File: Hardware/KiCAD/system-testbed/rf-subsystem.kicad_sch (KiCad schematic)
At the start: 42 parts, among them P3 Conn_Coaxial_UHF, U3 CC1200RHBR, U4 SKY13380-350LF, X1 40 MHz

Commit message: feat: begin dedicated sheets for RF switch throws, refine PA RFIC symbol #34
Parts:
- removed U4: SKY13380-350LF, Package_DFN_QFN:QFN-16-1EP_3x3mm_P0.5mm_EP1.7x1.7mm, symbol RF_Switch:SKY13380-350LF
- added FL1: LFCN-490, Filter:Filter_Mini-Circuits_FV1206, symbol RF_Filter:LFCN-490
- added FL2: LFCN-160, Filter:Filter_Mini-Circuits_FV1206, symbol RF_Filter:LFCN-160
- P3: value Conn_Coaxial_UHF -> SMA
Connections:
- net RF_{TRX} is gone; now on an unnamed net: C177.2, L174.2
- net VDD is gone; now on net +3.3V: C171.1, C172.1, C173.1, R171.1
- net GND: now also FL1.2 (GND), FL1.4 (GND), FL2.2 (GND), FL2.4 (GND)
- net UHF 6W PA/RF_{OUT}: now also FL1.1 (IN)
- net RF Switch/RFSW_{POLE}: now reaches P3.1 (In)
- net RF Switch/RFSW_{POLE}: no longer R181.1
- net RF_Signal: no longer names the net of R181.2
- new net TRX_{RF}: R181.1
- new net TX_{UHF}: FL1.3 (OUT)
- new net TX_{VHF}: FL2.3 (OUT)
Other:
- sheet RF Power Amplifier renamed UHF 6W PA
- added sheet RF Switch (rf-switch.kicad_sch)
- added sheet VHF 6W PA (rf-power-amplifier-vhf.kicad_sch)
- sheet UHF 6W PA: file rf-power-amplifier.kicad_sch -> rf-power-amplifier-uhf.kicad_sch
- note added: "RF Frontend for UHF Reference 420-470 MHz Tune"
- note added: "TRX_GPIO3 can be used to control an external LNA, PA, or RX/TX switch. HIGH in Sleep, Active LOW"
- note removed: "Antenna"
- note removed: "RF Frontend"
- note removed: "TRX_GPIO3 can be used to control an external LNA, PA, or RX/TX switch."
- moved on the sheet: P3, R181

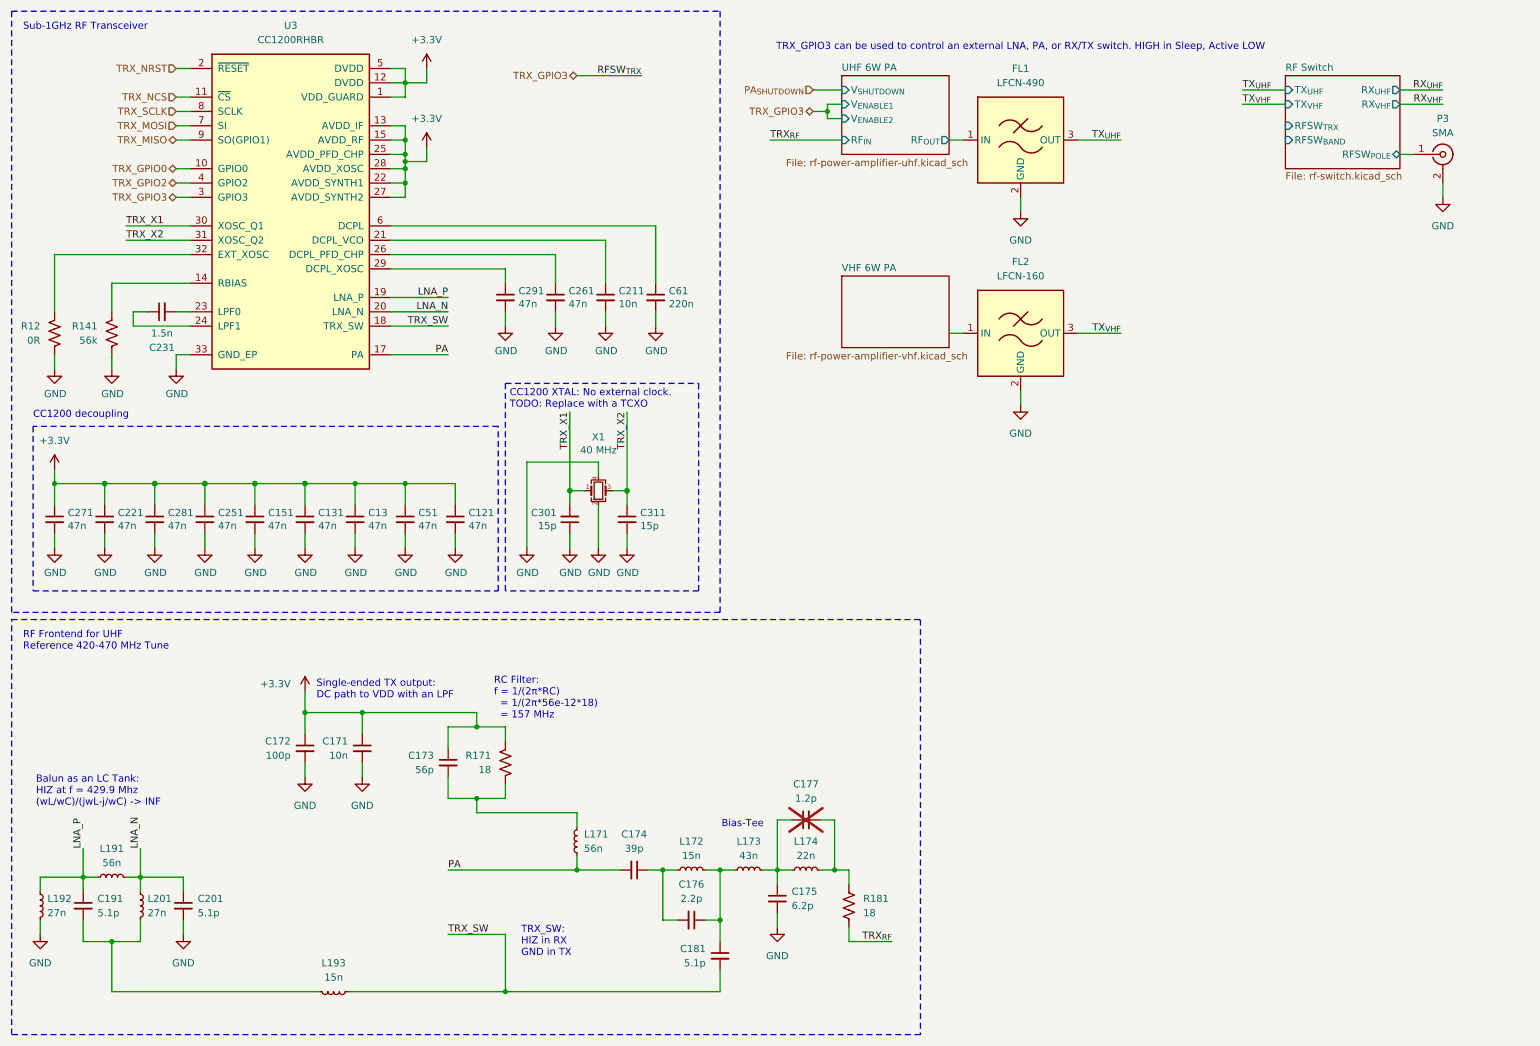
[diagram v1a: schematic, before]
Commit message: feat: refine rf subsystem sheet, specify band selection from two tuned PAs #34
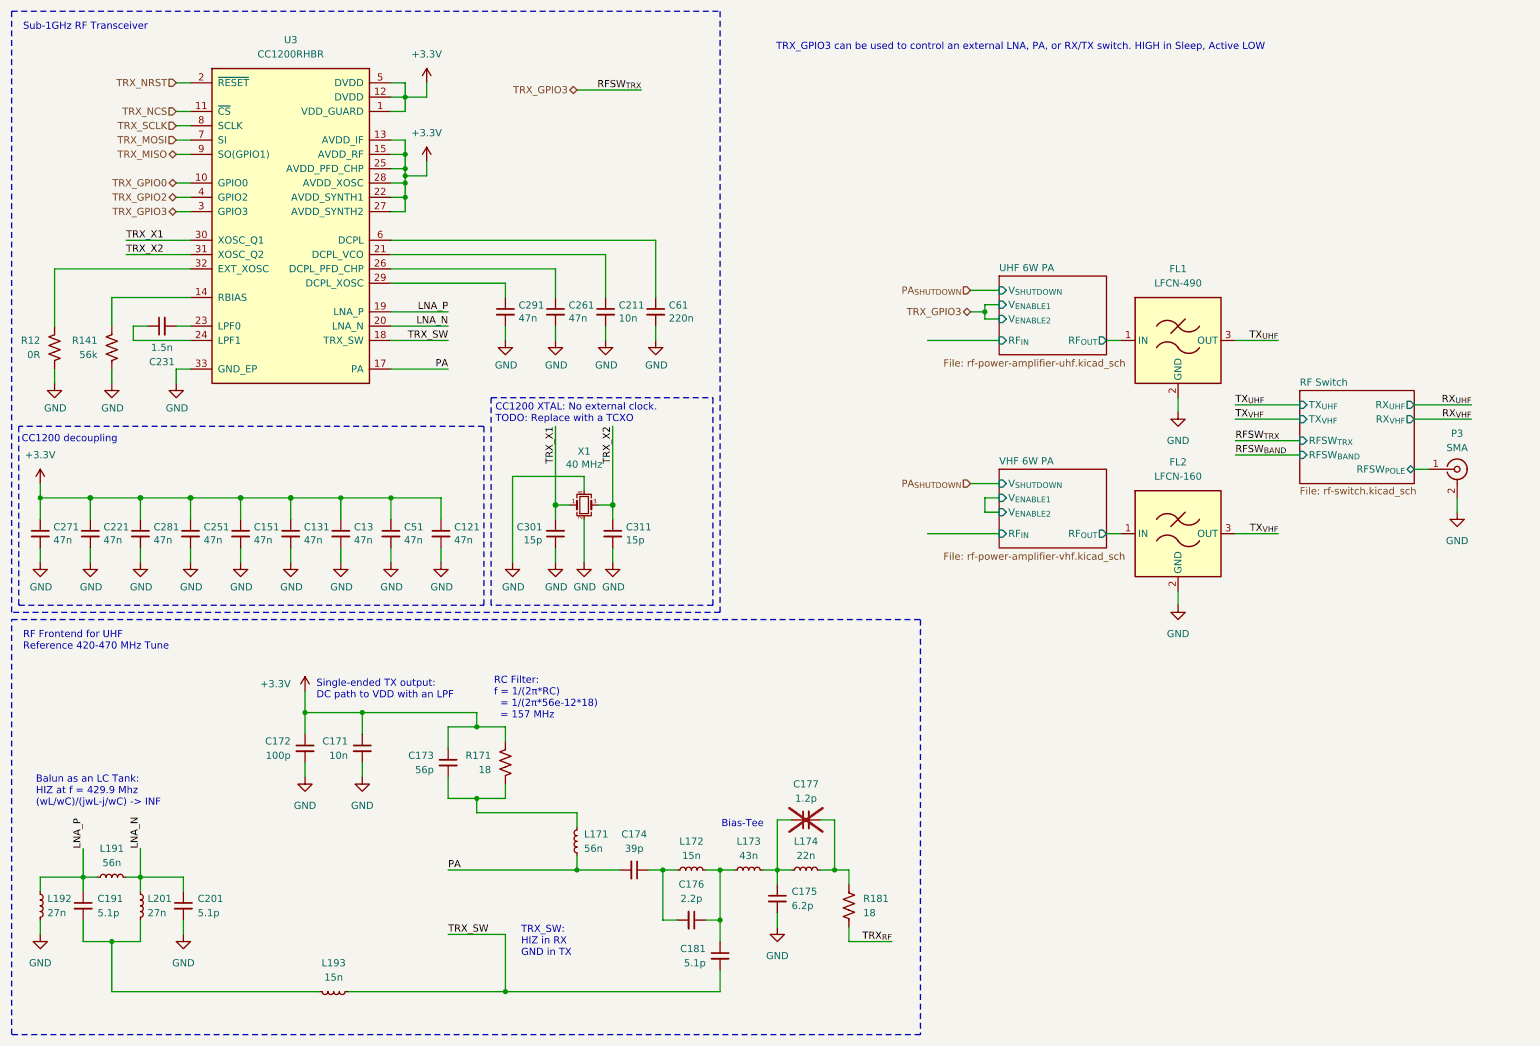
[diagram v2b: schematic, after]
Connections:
- net VHF 6W PA/RF_{OUT}: now reaches FL2.1 (IN)
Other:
- sheet VHF 6W PA ports: added RF_{IN}, RF_{OUT}, V_{ENABLE1}, V_{ENABLE2}, V_{SHUTDOWN}; removed none
- moved on the sheet: C121, C13, C131, C151, C211, C221, C231, C251, C261, C271, C281, C291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

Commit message: feat: complete RF switches, revise RF sheet structure #34
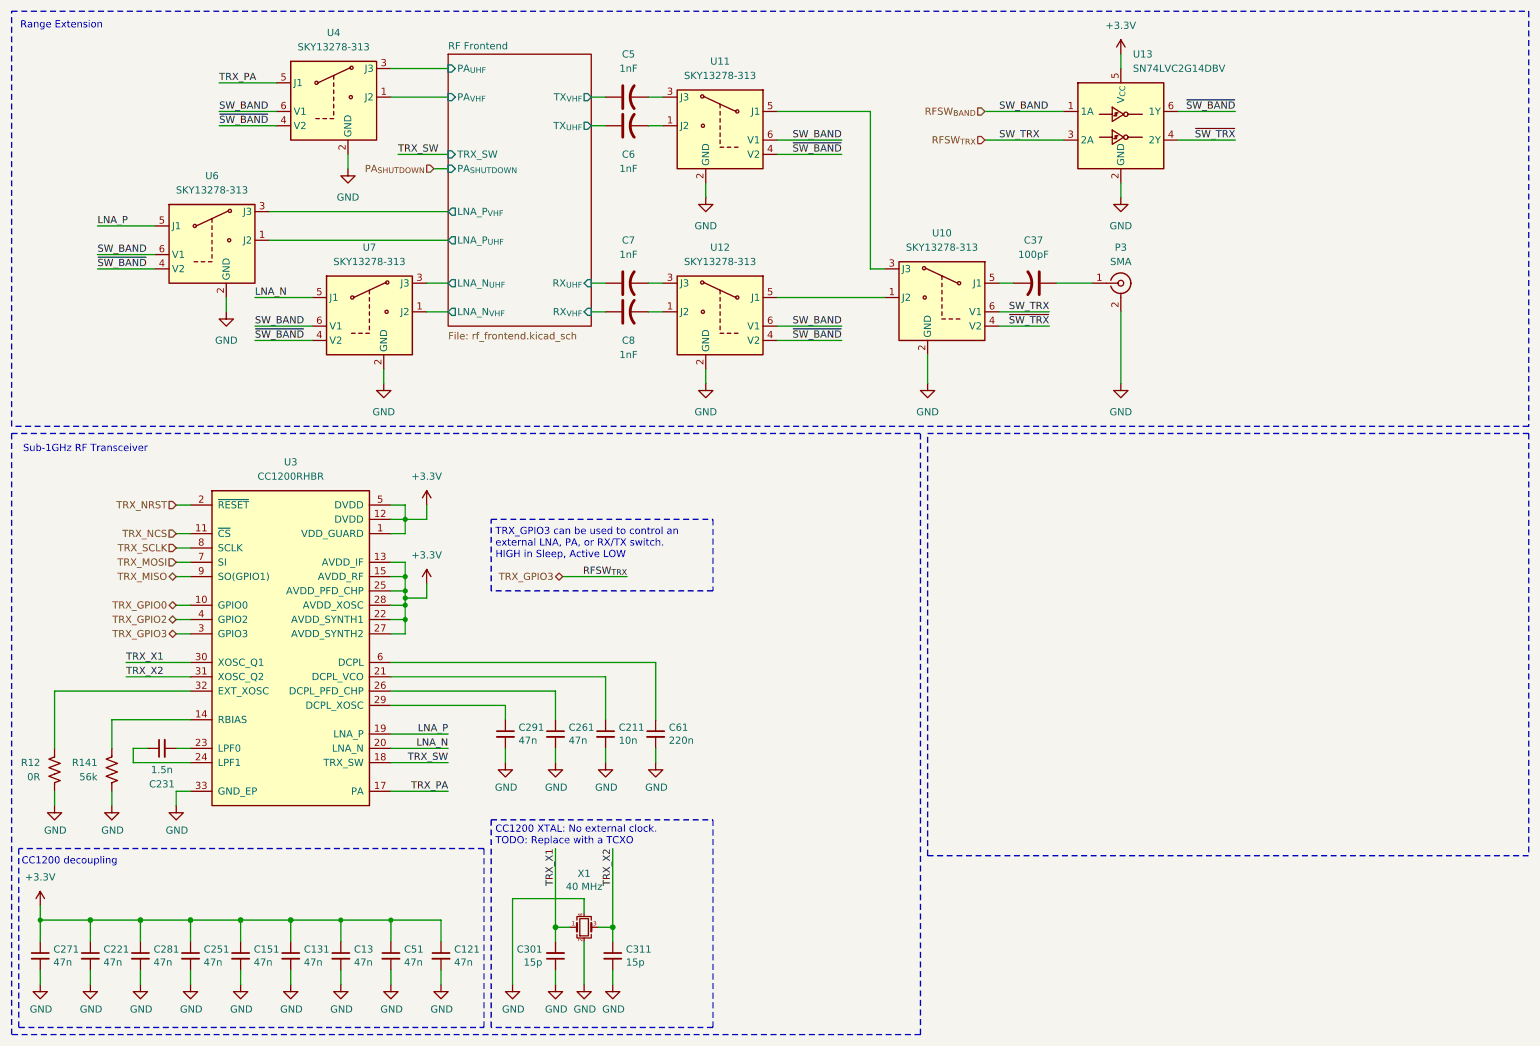
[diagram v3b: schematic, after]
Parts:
- removed C171: 10n, Capacitor_SMD:C_0402_1005Metric, symbol Device:C_Small
- removed C172: 100p, Capacitor_SMD:C_0402_1005Metric, symbol Device:C_Small
- removed C173: 56p, Capacitor_SMD:C_0402_1005Metric, symbol Device:C_Small
- removed C174: 39p, Capacitor_SMD:C_0402_1005Metric, symbol Device:C_Small
- removed C175: 6.2p, Capacitor_SMD:C_0402_1005Metric, symbol Device:C_Small
- removed C176: 2.2p, Capacitor_SMD:C_0402_1005Metric, symbol Device:C_Small
- removed C177: 1.2p, Capacitor_SMD:C_0402_1005Metric, symbol Device:C_Small
- removed C181, C191, C201: 5.1p, Capacitor_SMD:C_0402_1005Metric, symbol Device:C_Small
- removed FL1: LFCN-490, Filter:Filter_Mini-Circuits_FV1206, symbol RF_Filter:LFCN-490
- removed FL2: LFCN-160, Filter:Filter_Mini-Circuits_FV1206, symbol RF_Filter:LFCN-160
- removed L171, L191: 56n, Inductor_SMD:L_0402_1005Metric, symbol Device:L_Small
- removed L172, L193: 15n, Inductor_SMD:L_0402_1005Metric, symbol Device:L_Small
- removed L173: 43n, Inductor_SMD:L_0402_1005Metric, symbol Device:L_Small
- removed L174: 22n, Inductor_SMD:L_0402_1005Metric, symbol Device:L_Small
- removed L192, L201: 27n, Inductor_SMD:L_0402_1005Metric, symbol Device:L_Small
- removed R171, R181: 18, Resistor_SMD:R_0402_1005Metric, symbol Device:R_US
- added C37: 100pF, symbol Device:C_US
- added C5, C6, C7, C8: 1nF, symbol Device:C_US
- added U10, U11, U12, U4, U6, U7: SKY13278-313, symbol capstone-project:SKY13278-313
- added U13: SN74LVC2G14DBV, Package_TO_SOT_SMD:SOT-23-6, symbol 74xGxx:SN74LVC2G14DBV
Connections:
- net +3.3V: now also U13.5 (V_{CC})
- net GND: now also U10.2 (GND), U11.2 (GND), U12.2 (GND), U13.2 (GND), U4.2 (GND), U6.2 (GND), U7.2 (GND)
- net LNA_N: now also U7.5 (J1)
- net LNA_P: now also U6.5 (J1)
- net RFSW_{BAND}: now also U11.6 (V1), U12.6 (V1), U13.1 (1A), U4.6 (V1), U6.6 (V1), U7.6 (V1)
- net PA renamed TRX_PA
- net TRX_PA: now also U4.5 (J1)
- net RF Switch/RFSW_{POLE}: no longer names the net of P3.1 (In)
- net RF Switch/RFSW_{POLE}: now also C37.1
- net TRX_GPIO3 renamed RFSW_{TRX}
- net RFSW_{TRX}: now also U10.6 (V1), U13.3 (2A)
- new net: U10.1 (J2), U12.5 (J1)
- new net: U10.3 (J3), U11.5 (J1)
- new net: C37.2, U10.5 (J1)
- new net: C5.2, U11.3 (J3)
- new net: C8.2, U12.1 (J2)
- new net: C6.2, U11.1 (J2)
- new net: C7.2, U12.3 (J3)
- new net RF Frontend/LNA_N_{UHF}: U7.3 (J3)
- new net RF Frontend/LNA_N_{VHF}: U7.1 (J2)
- new net RF Frontend/LNA_P_{UHF}: U6.1 (J2)
- new net RF Frontend/LNA_P_{VHF}: U6.3 (J3)
- new net RF Frontend/PA_{UHF}: U4.3 (J3)
- new net RF Frontend/PA_{VHF}: U4.1 (J2)
- new net RF Frontend/RX_{UHF}: C7.1
- new net RF Frontend/RX_{VHF}: C8.1
- new net RF Frontend/TX_{UHF}: C6.1
- new net RF Frontend/TX_{VHF}: C5.1
- new net ~{SW_BAND}: U11.4 (V2), U12.4 (V2), U13.6 (1Y), U4.4 (V2), U6.4 (V2), U7.4 (V2)
- new net ~{SW_TRX}: U10.4 (V2), U13.4 (2Y)
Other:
- removed sheet RF Switch
- removed sheet UHF 6W PA
- removed sheet VHF 6W PA
- added sheet RF Frontend (rf_frontend.kicad_sch)
- note added: "Range Extension"
- note removed: "Balun as an LC Tank: HIZ at f = 429.9 Mhz (wL/wC)/(jwL-j/wC) -> INF"
- note removed: "Bias-Tee"
- note removed: "RC Filter: f = 1/(2π*RC) = 1/(2π*56e-12*18) = 157 MHz"
- note removed: "RF Frontend for UHF Reference 420-470 MHz Tune"
- note removed: "Single-ended TX output: DC path to VDD with an LPF"
- note removed: "TRX_SW: HIZ in RX GND in TX"
- moved on the sheet: C121, C13, C131, C151, C211, C221, C231, C251, C261, C271, C281, C291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
